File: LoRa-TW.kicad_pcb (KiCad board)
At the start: 4 copper layers, 15 x 26.6 mm, 48 parts, among them J1 MHF-I/U.FL, J2 Conn_02x06_2.0mm, J3 RFShield_OnePiece, U1 SX1262IMLTRT, X1 TCXO, 32MHz, 2.0x1.6mm

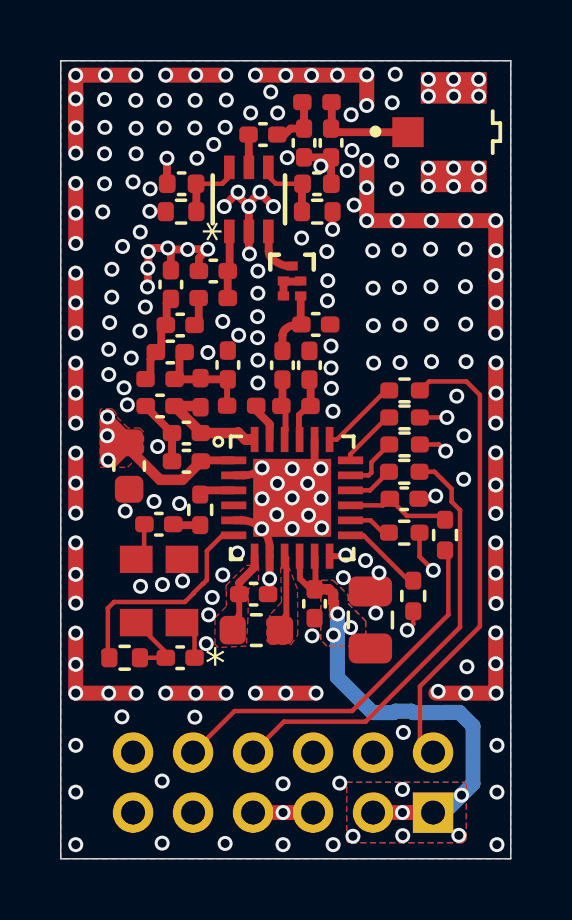
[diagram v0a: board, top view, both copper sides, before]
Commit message: update 15uH for sch and pcb
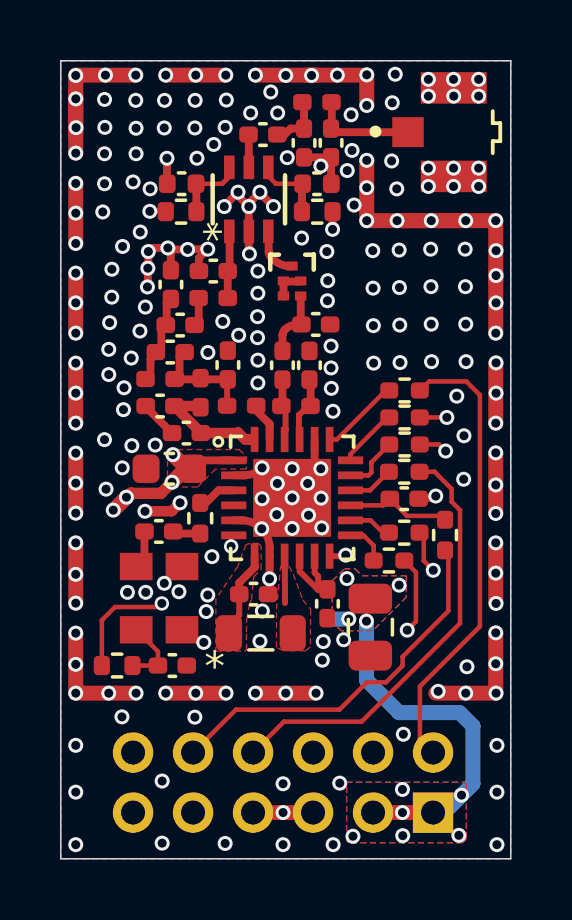
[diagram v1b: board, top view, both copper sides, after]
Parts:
- removed the C20 at (151.3, 101.0)
- L7: footprint Inductor_SMD:L_0603_1608Metric -> Inductor_SMD:L_0805_2012Metric
- moved R10 1.43 mm to (158.0, 104.4), turned to 0 degrees
- moved C21 1.34 mm to (150.7, 101.3), turned to 180 degrees
- moved C19 0.43 mm to (156.0, 105.8)
- moved C2 0.37 mm to (150.8, 107.9)
- moved FB1 0.36 mm to (148.9, 107.9)
- moved R1 0.28 mm to (151.7, 103.0)
- moved C1 0.24 mm to (150.3, 103.4)
- moved C20 0.24 mm to (157.4, 106.6), turned to 90 degrees
- moved X1 0.24 mm to (150.3, 105.6)
- moved L7 0.18 mm to (153.7, 106.8)
- renumbered C22 to C20
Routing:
- net VDD: track 48.3 -> 42.6 mm, vias 13 -> 15
- net Net-(J2-Pin_9): track 10.9 -> 12.8 mm
- net /DIO1_INT: track 2.79 -> 1.49 mm
- net Net-(U1-DCC_SW): track 2.50 -> 1.57 mm
- net GND: track 23.5 -> 23.1 mm, vias 219 -> 222
- net /DIO3_CLK_{EN}: track 7.73 -> 8.01 mm, vias 0 -> 2
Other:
- board text added: "0"
- board text added: "0 mm"
- board text added: "0.005 mm"
- board text added: "0.0152 mm"
- board text added: "0.02"
- board text added: "0.035 mm"
- board text added: "0.1524 mm / 0.1524 mm"
- board text added: "0.2104 mm"
- board text added: "0.3000 mm"
- board text added: "1"
- board text added: "1.065 mm"
- board text added: "1.5962 mm"
- board text added: "100 Ohm coplanar differential: 0.1547 mm / 0.1524 mm / 0.1524 mm"
- board text added: "15.0000 mm x 26.6000 mm"
- board text added: "3.3"
- board text added: "4"
- board text added: "4.5"
- board text added: "50 Ohm coplanar single end: 0.2634 mm / 0.1524 mm"
- board text added: "7628"
- board text added: "B.Cu"
- board text added: "B.Mask"
- board text added: "B.Paste"
- board text added: "B.Silkscreen"
- board text added: "BOARD CHARACTERISTICS"
- board text added: "Board Thickness:"
- board text added: "Board overall dimensions:"
- board text added: "Bottom Silk Screen"
- board text added: "Bottom Solder Mask"
- board text added: "Bottom Solder Paste"
- board text added: "Castellated pads:"
- board text added: "Color"
- board text added: "Copper Finish:"
- board text added: "Copper Layer Count:"
- board text added: "Dielectric 1"
- board text added: "Dielectric 2"
- board text added: "Dielectric 3"
- board text added: "Edge card connectors:"
- board text added: "Epsilon R"
- board text added: "F.Cu"
- board text added: "F.Mask"
- board text added: "F.Paste"
- board text added: "F.Silkscreen"
- board text added: "FR4"
- board text added: "FR4 natural"
- board text added: "HAL SnPb"
- board text added: "IMPEDANCE CONTROL"
- board text added: "Impedance Control:"
- board text added: "In1.Cu"
- board text added: "In2.Cu"
- board text added: "Layer Name"
- board text added: "Loss Tangent"
- board text added: "Material"
- board text added: "Min hole diameter:"
- board text added: "Min track/spacing:"
- board text added: "No"
- board text added: "Not specified"
- board text added: "Plated Board Edge:"
- board text added: "STACKUP: JLC04161H-7628"
- board text added: "Thickness (mm)"
- board text added: "Top Silk Screen"
- board text added: "Top Solder Mask"
- board text added: "Top Solder Paste"
- board text added: "Type"
- board text added: "Yes"
- board text added: "copper"
- board text added: "core"
- board text added: "prepreg"

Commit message: prepare for BOM generation
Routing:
- net GND: track 23.1 -> 21.6 mm, vias 222 -> 234
- net Net-(U1-DCC_SW): track 1.57 -> 2.70 mm
- net VDD: track 42.6 -> 41.6 mm
- added copper zone on F.Cu, net Net-(U1-VR_PA)

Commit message: update footprint of PCB for DRC check and fine turning
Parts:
- FL1: footprint LoRa-TW:IC5_B39931B2645P810_QUA -> LoRa-TW:B39931B2645P810_QUA
- moved C2 1.87 mm to (148.9, 107.8), turned to 0 degrees
- moved FB1 1.80 mm to (150.8, 107.8), turned to 0 degrees
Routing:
- net /DIO3_CLK_{EN}: track 8.01 -> 6.22 mm
- net GND: track 21.6 -> 21.9 mm, vias 234 -> 239

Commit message: sych. properties of schematic to pcb
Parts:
- C1: value 10P -> 10p
- C6, C7: footprint Capacitor_SMD:C_0402_1005Metric -> LoRa-TW:C_HF_0402_1005Metric
- FB1, R2, R3: footprint Resistor_SMD:R_0402_1005Metric -> LoRa-TW:R_HF_0402_1005Metric
- FL1: footprint LoRa-TW:B39931B2645P810_QUA -> LoRa-TW:IC5_B39931B2645P810_QUA
- R10, R4, R5, R6, R7, R8, R9: value 33 -> 22

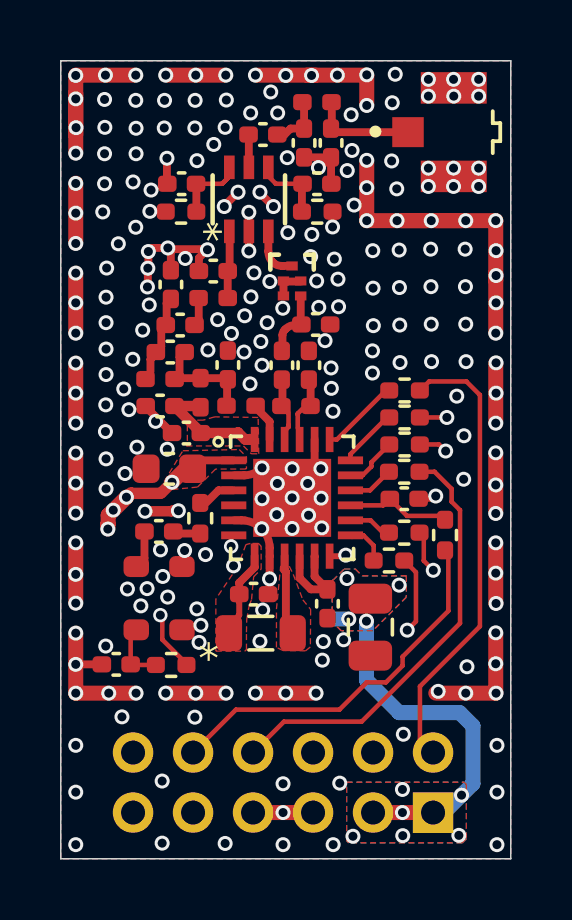
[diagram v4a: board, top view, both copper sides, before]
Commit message: optimization DC2DC layout
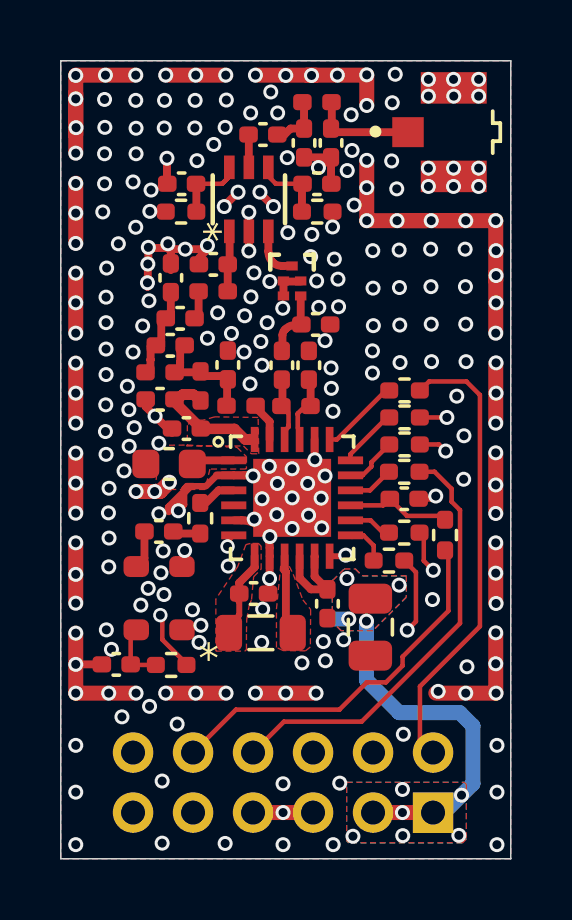
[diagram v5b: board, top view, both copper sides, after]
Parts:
- moved C13 0.23 mm to (151.1, 96.3)
- moved L4 0.23 mm to (150.4, 98.1)
- moved C10 0.22 mm to (150.7, 97.2)
- moved C12 0.22 mm to (150.7, 94.9)
- moved C14 0.22 mm to (152.2, 94.5)
- moved C9 0.22 mm to (150.4, 99.0)
- moved L3 0.22 mm to (151.7, 98.5)
- moved L5 0.22 mm to (152.2, 95.4)
- moved C21 0.16 mm to (150.7, 101.1)
- moved C8 0.15 mm to (151.3, 100.0)
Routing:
- net GND: track 21.9 -> 24.8 mm, vias 239 -> 248
- net VDD: track 41.6 -> 39.5 mm, vias 15 -> 14

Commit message: optimization layout
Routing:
- net Net-(U1-DCC_SW): track 2.70 -> 6.07 mm
- net VDD: track 39.5 -> 41.2 mm
- net GND: track 24.8 -> 26.1 mm, vias 248 -> 249
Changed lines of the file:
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@@
 	)
 	(segment
+		(start 156.1904 106.111343)
+		(end 156.128657 106.111343)
+		(width 0.1524)
+		(layer "F.Cu")
+		(net 3)
+	)
+	(segment
+		(start 156.1904 106.6904)
+		(end 156.1904 106.111343)
+		(width 0.1524)
+		(layer "F.Cu")
+		(net 3)
+	)
+	(segment
 		(start 149.9 99.23)
 		(end 150.78 100.11)
@@
 	)
 	(segment
+		(start 156.5 107)
+		(end 156.1904 106.6904)
+		(width 0.1524)
+		(layer "F.Cu")
+		(net 3)
+	)
+	(segment
 		(start 150.68 93.98)
 		(end 150.64 93.94)
@@
 	)
 	(segment
+		(start 156.128657 106.111343)
+		(end 155.96 106.28)
+		(width 0.1524)
+		(layer "F.Cu")
+		(net 3)
+	)
+	(segment
 		(start 150.64 93.94)
 		(end 150.11 93.94)
@@
 	)
 	(via
-		(at 154.47 95.95)
+		(at 154.45 95.95)
 		(size 0.5)
 		(drill 0.3)
@@
 	)
 	(via
+		(at 158.925502 106.393316)
+		(size 0.5)
+		(drill 0.3)
+		(layers "F.Cu" "B.Cu")
+		(free yes)
+		(net 3)
+	)
+	(via
 		(at 154.64 93.43)
 		(size 0.5)
@@
 	)
 	(via
-		(at 159.46 105.66)
+		(at 159.432073 105.334597)
 		(size 0.5)
 		(drill 0.3)
@@
 	)
 	(via
-		(at 155.821317 107.061317)
+		(at 155.89 107.1)
 		(size 0.5)
 		(drill 0.3)
@@
 	)
 	(via
-		(at 156.78 90.69)
+		(at 156.61 90.68)
 		(size 0.5)
 		(drill 0.3)
@@
 	)
 	(via
-		(at 156.62 91.36)
+		(at 156.51 91.35)
 		(size 0.5)
 		(drill 0.3)
@@
 	)
 	(via
-		(at 149.29 98.55)
+		(at 149.24 98.58)
 		(size 0.5)
 		(drill 0.3)
@@
 	)
 	(via
-		(at 155.66 91.26)
+		(at 156.65 91.94)
 		(size 0.5)
 		(drill 0.3)
@@
 	)
 	(via
-		(at 154.62 90.93)
+		(at 154.66 90.87)
 		(size 0.5)
 		(drill 0.3)
@@
 	)
 	(via
-		(at 156.144225 99.384413)
+		(at 156.16 99.384413)
 		(size 0.5)
 		(drill 0.3)
@@
 	)
 	(via
-		(at 156.75 89.5)
+		(at 156.79 89.5)
 		(size 0.5)
 		(drill 0.3)
@@
 	)
 	(segment
+		(start 156.67 106.079988)
+		(end 156.67 106.31)
+		(width 0.2634)
+		(layer "F.Cu")
+		(net 14)
+	)
+	(segment
 		(start 150.32 102.12)
 		(end 150.69 101.75)
@@
 	)
 	(segment
+		(start 155.96 105.32)
+		(end 155.77 105.51)
+		(width 0.2634)
+		(layer "F.Cu")
+		(net 14)
+	)
+	(segment
 		(start 159 102.3)
 		(end 159.48 102.3)
@@
 	)
 	(segment
+		(start 155.77 105.51)
+		(end 155.77 105.67)
+		(width 0.2634)
+		(layer "F.Cu")
+		(net 14)
+	)
+	(segment
 		(start 159.48 102.3)
 		(end 159.57 102.21)
@@
 	)
 	(segment
+		(start 156.274912 105.6849)
+		(end 156.67 106.079988)
+		(width 0.2634)
+		(layer "F.Cu")
+		(net 14)
+	)
+	(segment
 		(start 151.465 101.3)
 		(end 151.23 101.3)
@@
 	)
 	(segment
+		(start 155.77 105.67)
+		(end 155.7849 105.6849)
+		(width 0.2634)
+		(layer "F.Cu")
+		(net 14)
+	)
+	(segment
 		(start 155.0325 104.9425)
 		(end 155.0325 104.215125)
@@
 	)
 	(segment
+		(start 155.7849 105.6849)
+		(end 156.274912 105.6849)
+		(width 0.2634)
+		(layer "F.Cu")
+		(net 14)
+	)
+	(segment
 		(start 155.56 104.242625)
 		(end 155.5325 104.215125)
@@
 	)
 	(segment
+		(start 154.5325 104.215125)
+		(end 154.5325 104.987114)
+		(width 0.2)
+		(layer "F.Cu")
+		(net 31)
+	)
+	(segment
+		(start 155.355386 105.81)
+		(end 155.36 105.81)
+		(width 0.2)
+		(layer "F.Cu")
+		(net 31)
+	)
+	(segment
+		(start 154.5325 104.987114)
+		(end 155.355386 105.81)
+		(width 0.2)
+		(layer "F.Cu")
+		(net 31)
+	)
+	(segment
 		(start 154.5751 106.5526)
 		(end 154.8025 106.78)
@@
 	)
 	(segment
+		(start 155.36 105.814614)
+		(end 155.36 107.24)
+		(width 0.2)
+		(layer "F.Cu")
+		(net 31)
+	)
+	(segment
 		(start 154.52 104.68)
 		(end 154.5751 104.7351)
@@
 	)
 	(segment
+		(start 155.355386 105.81)
+		(end 155.36 105.814614)
+		(width 0.2)
+		(layer "F.Cu")
+		(net 31)
+	)
+	(segment
 		(start 154.5325 104.215125)
 		(end 154.54 104.222625)
@@
 	)
 	(segment
-		(start 154.421743 108.25)
-		(end 156.047294 108.25)
+		(start 158.953473 105.126527)
+		(end 158.953473 105.363473)
 		(width 0.1524)
 		(layer "In2.Cu")
@@
 	)
 	(segment
-		(start 153.738257 109.28)
-		(end 154.0904 108.927857)
+		(start 159.487507 104.684556)
+		(end 159.395444 104.684556)
 		(width 0.1524)
 		(layer "In2.Cu")
@@
 	)
 	(segment
-		(start 156.047294 108.25)
-		(end 156.05712 108.259825)
+		(start 159.395444 104.684556)
+		(end 158.953473 105.126527)
 		(width 0.1524)
 		(layer "In2.Cu")
@@
 	)
 	(segment
-		(start 156.05712 108.259825)
-		(end 159.487507 104.829438)
+		(start 154.0904 108.581343)
+		(end 154.0904 108.927857)
 		(width 0.1524)
 		(layer "In2.Cu")
@@
 	)
 	(segment
-		(start 149.48 110.76)
-		(end 149.48 110.544863)
+		(start 153.738257 109.28)
+		(end 150.744863 109.28)
+		(width 0.1524)
+		(layer "In2.Cu")
+		(net 39)
+	)
+	(segment
+		(start 149.48 110.544863)
+		(end 149.48 110.76)
 		(width 0.1524)
 		(layer "In2.Cu")
@@
 	(segment
 		(start 154.0904 108.927857)
-		(end 154.0904 108.581343)
+		(end 153.738257 109.28)
 		(width 0.1524)
 		(layer "In2.Cu")
@@
 	)
 	(segment
-		(start 159.487507 104.829438)
-		(end 159.487507 104.684556)
+		(start 158.953473 105.363473)
+		(end 156.056945 108.26)
 		(width 0.1524)
 		(layer "In2.Cu")
@@
 	)
 	(segment
-		(start 150.744863 109.28)
-		(end 153.738257 109.28)
+		(start 154.411743 108.26)
+		(end 154.0904 108.581343)
 		(width 0.1524)
 		(layer "In2.Cu")
@@
 	)
 	(segment
-		(start 154.0904 108.581343)
-		(end 154.421743 108.25)
+		(start 156.056945 108.26)
+		(end 154.411743 108.26)
 		(width 0.1524)
 		(layer "In2.Cu")
@@
 	)
 	(segment
-		(start 149.48 110.544863)
-		(end 150.744863 109.28)
+		(start 150.744863 109.28)
+		(end 149.48 110.544863)
 		(width 0.1524)
 		(layer "In2.Cu")
@@
 	)
 	(segment
-		(start 158.91 106.39)
-		(end 158.62 106.68)
+		(start 158.45 106.84)
+		(end 158.46 106.84)
+		(width 0.1524)
+		(layer "F.Cu")
+		(net 40)
+	)
+	(segment
+		(start 158.91 104.75)
+		(end 158.91 105.66)
+		(width 0.1524)
+		(layer "F.Cu")
+		(net 40)
+	)
+	(segment
+		(start 158.91 105.66)
+		(end 158.42 106.15)
 		(width 0.1524)
 		(layer "F.Cu")
@@
 	)
 	(segment
-		(start 158.91 104.75)
-		(end 158.91 106.39)
+		(start 158.42 106.81)
+		(end 158.45 106.84)
+		(width 0.1524)
+		(layer "F.Cu")
+		(net 40)
+	)
+	(segment
+		(start 158.42 106.15)
+		(end 158.42 106.81)
 		(width 0.1524)
 		(layer "F.Cu")
@@
 	)
 	(via
-		(at 158.62 106.68)
+		(at 158.45 106.84)
 		(size 0.5)
 		(drill 0.3)
@@
 	)
 	(segment
-		(start 152.4322 111.8078)
-		(end 151.48 112.76)
+		(start 154.48 110.12)
+		(end 154.48 111.106615)
 		(width 0.1524)
 		(layer "In2.Cu")
@@
 	)
 	(segment
-		(start 154.48 110.12)
-		(end 154.48 111.106615)
+		(start 152.4322 111.8078)
+		(end 151.48 112.76)
 		(width 0.1524)
 		(layer "In2.Cu")
@@
 	)
 	(segment
-		(start 155.92 109.38)
-		(end 155.22 109.38)
+		(start 154.48 111.106615)
+		(end 153.778815 111.8078)
 		(width 0.1524)
 		(layer "In2.Cu")
@@
 	)
 	(segment
+		(start 158.45 106.84)
+		(end 158.45 106.85)
+		(width 0.1524)
+		(layer "In2.Cu")
+		(net 40)
+	)
+	(segment
 		(start 155.22 109.38)
 		(end 154.48 110.12)
@@
 	)
 	(segment
-		(start 158.62 106.68)
-		(end 155.92 109.38)
+		(start 155.92 109.38)
+		(end 155.22 109.38)
 		(width 0.1524)
 		(layer "In2.Cu")
@@
 	)
 	(segment
-		(start 154.48 111.106615)
-		(end 153.778815 111.8078)
+		(start 158.45 106.85)
+		(end 155.92 109.38)
 		(width 0.1524)
 		(layer "In2.Cu")

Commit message: update and fine turning
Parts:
- FL1: footprint LoRa-TW:IC5_B39931B2645P810_QUA -> LoRa-TW:SAW_1411
- moved C19 0.48 mm to (155.8, 105.3), turned to 0 degrees
- moved C20 0.28 mm to (157.2, 106.8), turned to 180 degrees
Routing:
- net GND: track 26.1 -> 78.9 mm, vias 249 -> 248
- net Net-(U1-DCC_SW): track 6.07 -> 10.8 mm
- net VDD: track 41.2 -> 44.9 mm, vias 14 -> 16
- net Net-(J2-Pin_6): track 13.0 -> 14.4 mm
- net Net-(J2-Pin_9): track 12.9 -> 13.5 mm

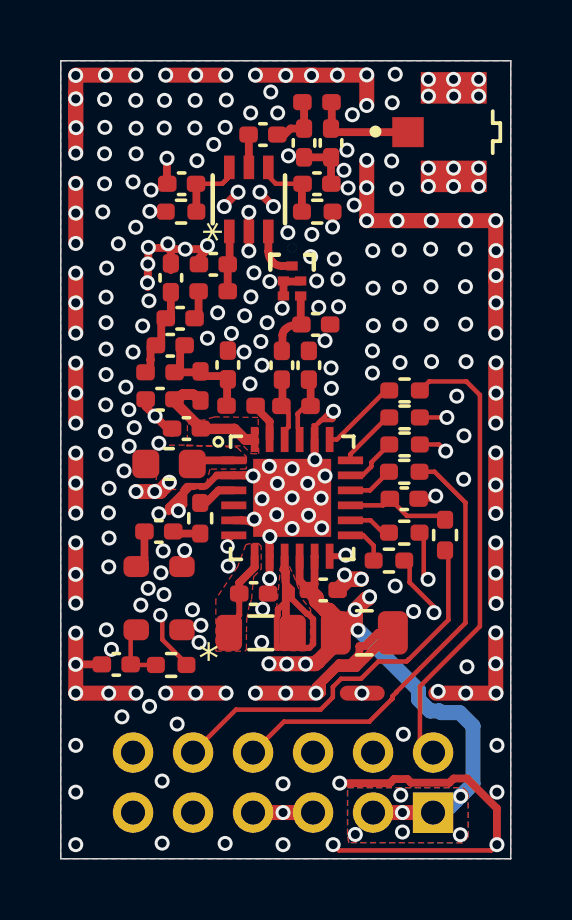
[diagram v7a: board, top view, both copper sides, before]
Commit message: PCB release version
Add LCSC part number into footprint properties
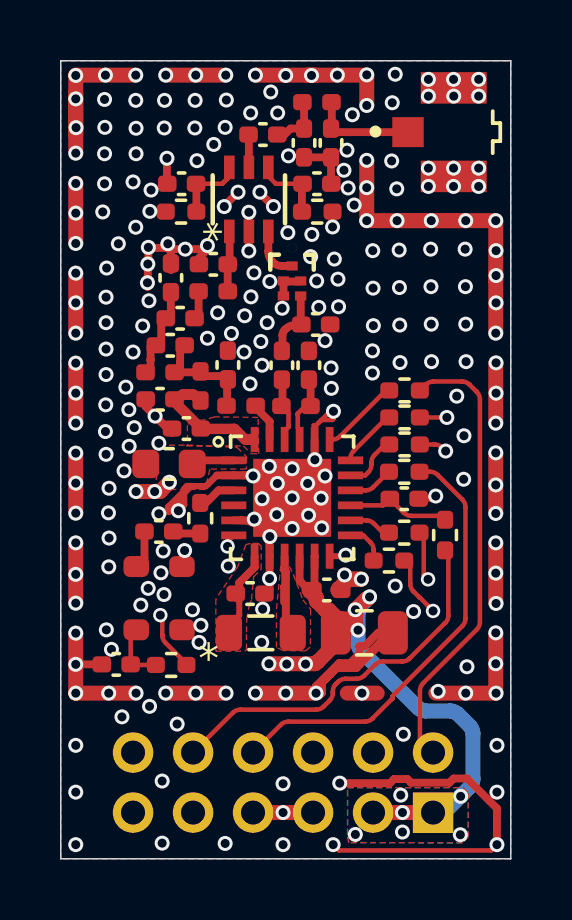
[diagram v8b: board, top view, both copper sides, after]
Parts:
- moved C18 0.12 mm to (153.4, 105.5)
- moved C19 0.12 mm to (155.9, 105.3)
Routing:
- net Net-(U1-DCC_SW): track 10.8 -> 5.21 mm
- net VDD: track 44.9 -> 45.5 mm
